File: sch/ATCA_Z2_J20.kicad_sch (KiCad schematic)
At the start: 1 part, among them J20 TE_64690XX-1_J20

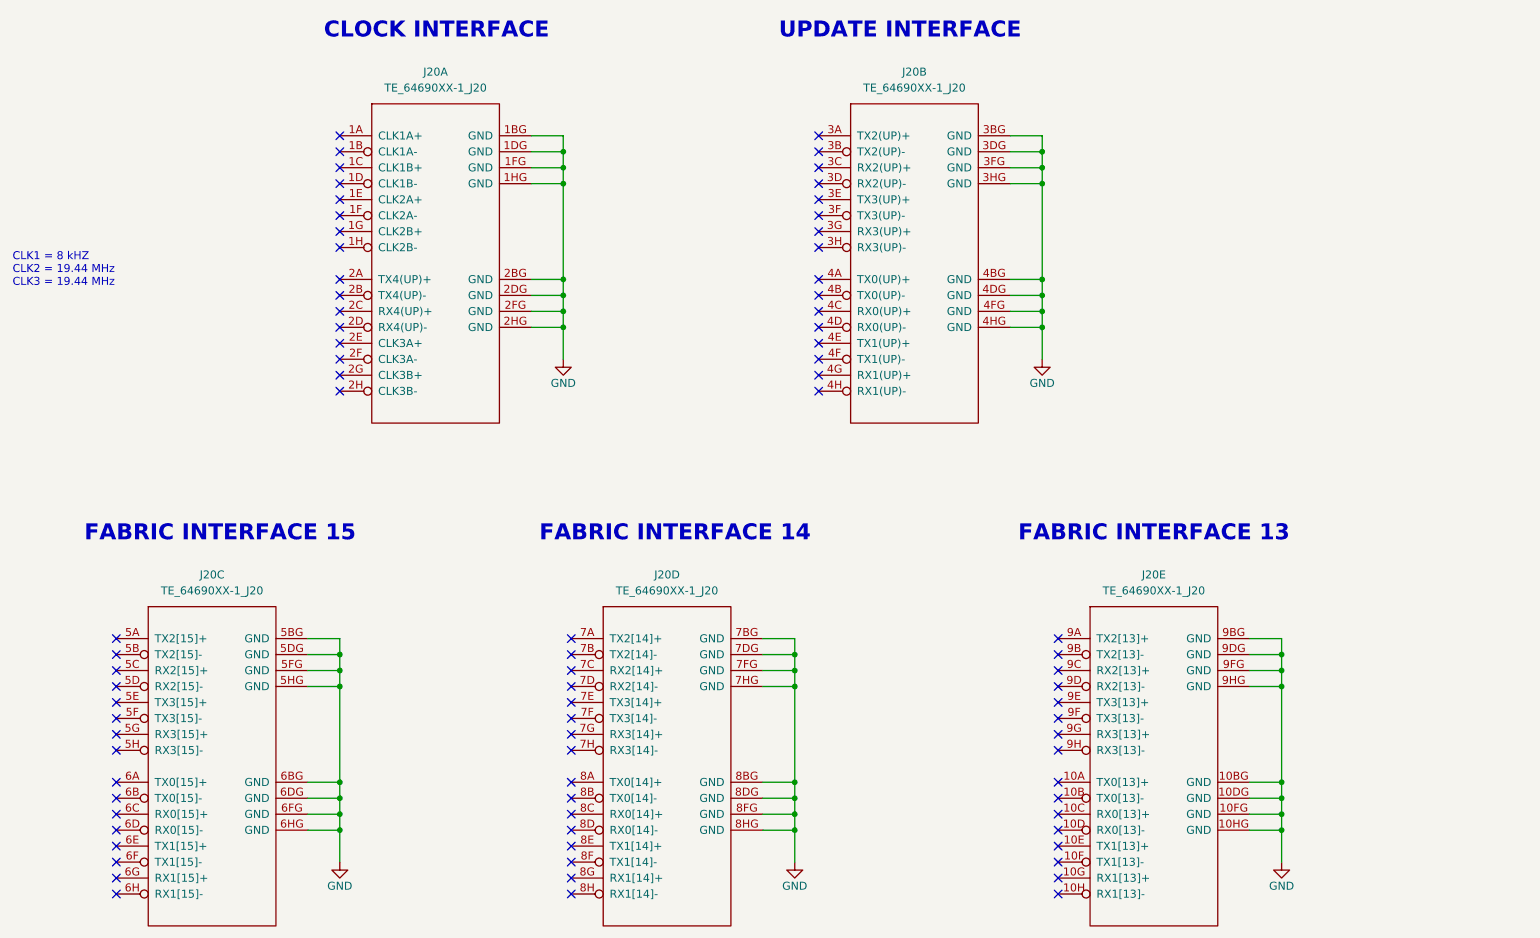
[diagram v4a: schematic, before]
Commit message: adding clks and fiber sheets
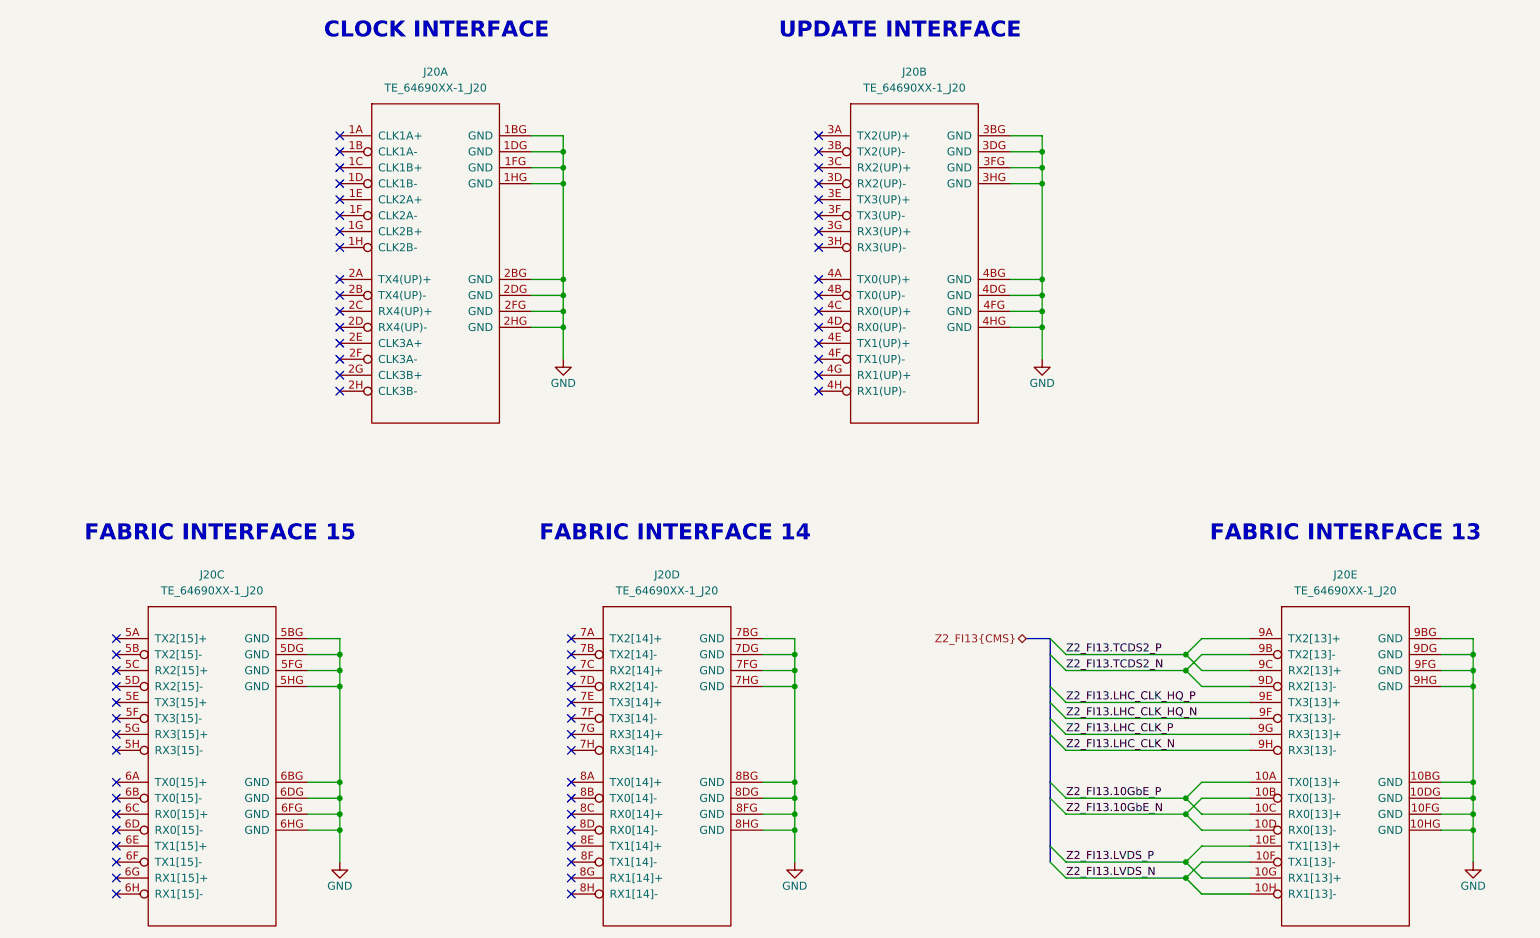
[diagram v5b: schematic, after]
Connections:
- net Z2_FI13.10GbE_P: now reaches J20.10A (TX0[13]+)
- net Z2_FI13.10GbE_P: now also J20.10C (RX0[13]+)
- net Z2_FI13.10GbE_N: now reaches J20.10B (TX0[13]-)
- net Z2_FI13.10GbE_N: now also J20.10D (RX0[13]-)
- net Z2_FI13.LVDS_P: now reaches J20.10E (TX1[13]+)
- net Z2_FI13.LVDS_P: now also J20.10G (RX1[13]+)
- net Z2_FI13.LVDS_N: now reaches J20.10F (TX1[13]-)
- net Z2_FI13.LVDS_N: now also J20.10H (RX1[13]-)
- net Z2_FI13.TCDS2_P: now reaches J20.9A (TX2[13]+)
- net Z2_FI13.TCDS2_P: now also J20.9C (RX2[13]+)
- net Z2_FI13.TCDS2_N: now reaches J20.9B (TX2[13]-)
- net Z2_FI13.TCDS2_N: now also J20.9D (RX2[13]-)
- net Z2_FI13.LHC_CLK_HQ_P: now reaches J20.9E (TX3[13]+)
- net Z2_FI13.LHC_CLK_HQ_N: now reaches J20.9F (TX3[13]-)
- net Z2_FI13.LHC_CLK_P: now reaches J20.9G (RX3[13]+)
- net Z2_FI13.LHC_CLK_N: now reaches J20.9H (RX3[13]-)
- no-connect marks 80 -> 64
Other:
- note removed: "CLK1 = 8 kHZ CLK2 = 19.44 MHz CLK3 = 19.44 MHz"
- moved on the sheet: J20E
